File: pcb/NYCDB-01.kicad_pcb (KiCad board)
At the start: 2 copper layers, 266 parts, among them J1 AUDIO_JACK, P1 CONN_BATT, P2 USB_OTG, Q1 Q_PMOS_GSD, SW1 SW_POWER, SW2 SW_RESET, U1 CS5361, U10 OPA4134, U11 TPA6120A2, U12 24C16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

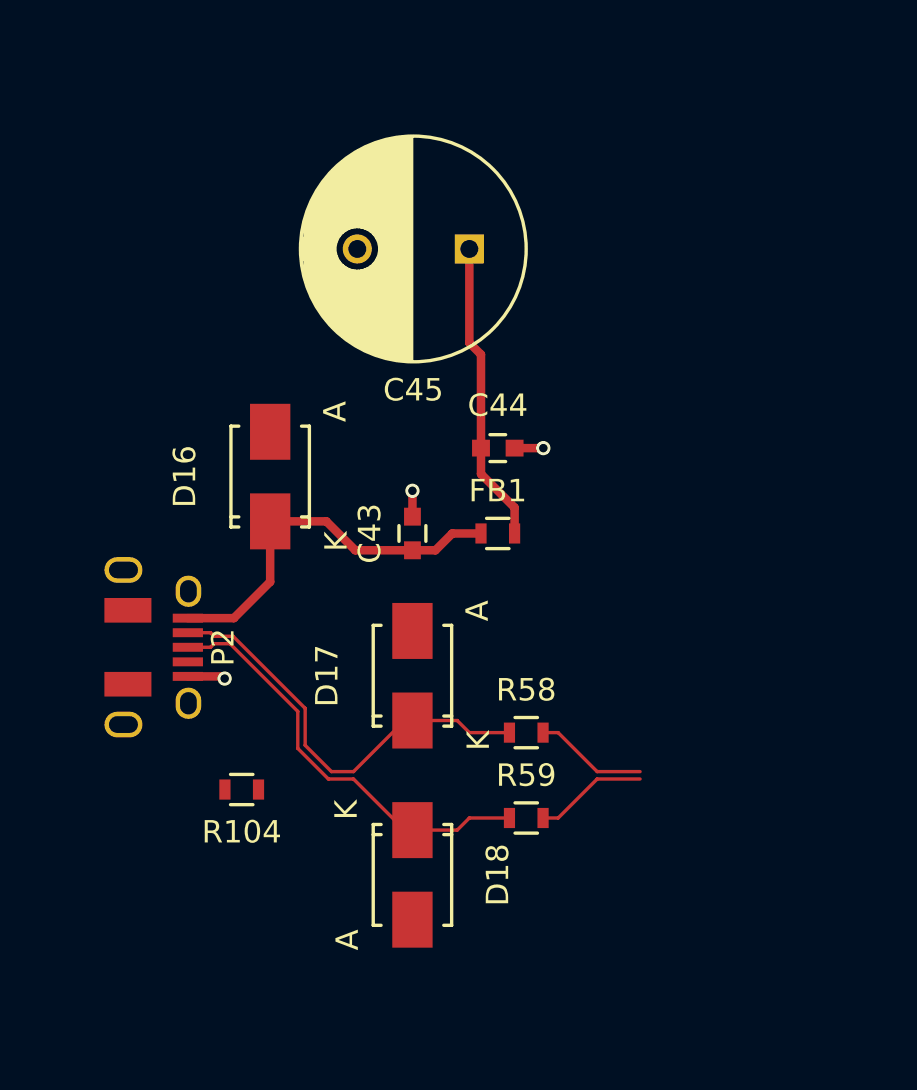
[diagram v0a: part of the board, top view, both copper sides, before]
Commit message: Worked on the USB connection
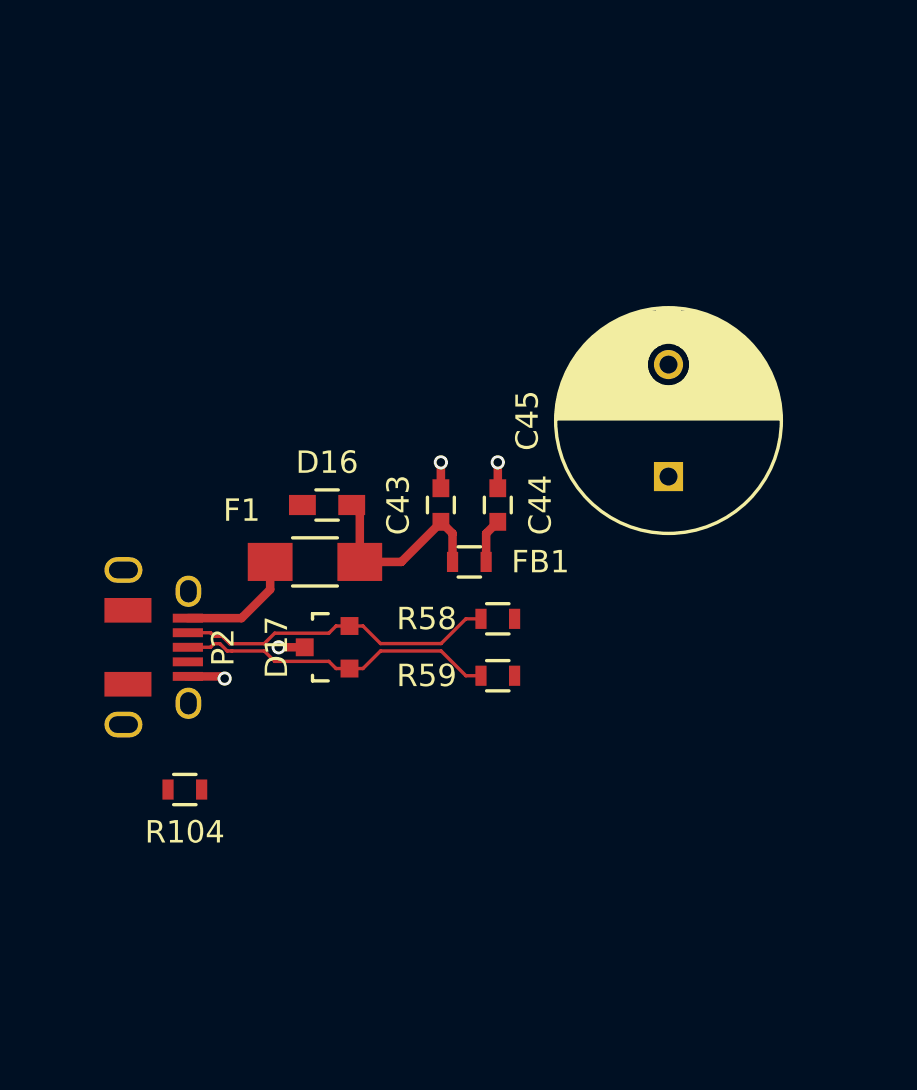
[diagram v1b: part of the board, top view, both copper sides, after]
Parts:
- removed D18: SMAJ5.0CA, Diodes_SMD:SMA_Standard
- added F1: 1206L150, Resistors_SMD:R_1206_HandSoldering, F.Cu at (172.2, 191.8)
- D16: value SMAJ5.0CA -> V5.5MLA0603H; footprint Diodes_SMD:SMA_Standard -> Resistors_SMD:R_0603_HandSoldering
- D17: value SMAJ5.0CA -> TVS_SOT23; footprint Diodes_SMD:SMA_Standard -> TO_SOT_Packages_SMD:SOT-23
- moved C45 13.5 mm to (188.0, 188.0), turned to 90 degrees
- moved R59 6.48 mm to (180.3, 196.8)
- moved R58 5.24 mm to (180.3, 194.3)
- moved D17 4.02 mm to (172.7, 195.6)
- moved D16 2.84 mm to (172.7, 189.2), turned to 0 degrees
- moved C44 2.54 mm to (180.3, 189.2), turned to 270 degrees
- moved R104 2.54 mm to (166.4, 201.9)
- moved C43 1.80 mm to (177.8, 189.2)
- moved FB1 1.80 mm to (179.1, 191.8), turned to 180 degrees
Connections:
- C44 pad 1: /FT2232D/USB5V -> GND
- C44 pad 2: GND -> /FT2232D/USB5V
- D16 pad 1: Net-(C43-Pad1) -> GNDPWR
- D16 pad 2: GNDPWR -> Net-(C43-Pad1)
- D17 pad 1: /USB Connector/CON_D- -> /USB Connector/CON_D+
- D17 pad 2: GNDPWR -> /USB Connector/CON_D-
- FB1 pad 1: Net-(C43-Pad1) -> /FT2232D/USB5V
- FB1 pad 2: /FT2232D/USB5V -> Net-(C43-Pad1)
- P2 pad 1: Net-(C43-Pad1) -> Net-(F1-Pad1)
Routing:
- net /FT2232D/USB5V: track 19.9 -> 8.37 mm
- net Net-(C43-Pad1): track 17.3 -> 9.07 mm
- net Net-(F1-Pad1): track 0.00 -> 5.44 mm
- net /FT2232D/D-: track 5.05 -> 0.00 mm
- net /FT2232D/D+: track 5.05 -> 0.00 mm
- net /USB Connector/CON_D+: track 19.1 -> 14.4 mm
- net /USB Connector/CON_D-: track 19.1 -> 14.4 mm
- net GNDPWR: track 0.00 -> 1.16 mm, vias 0 -> 1

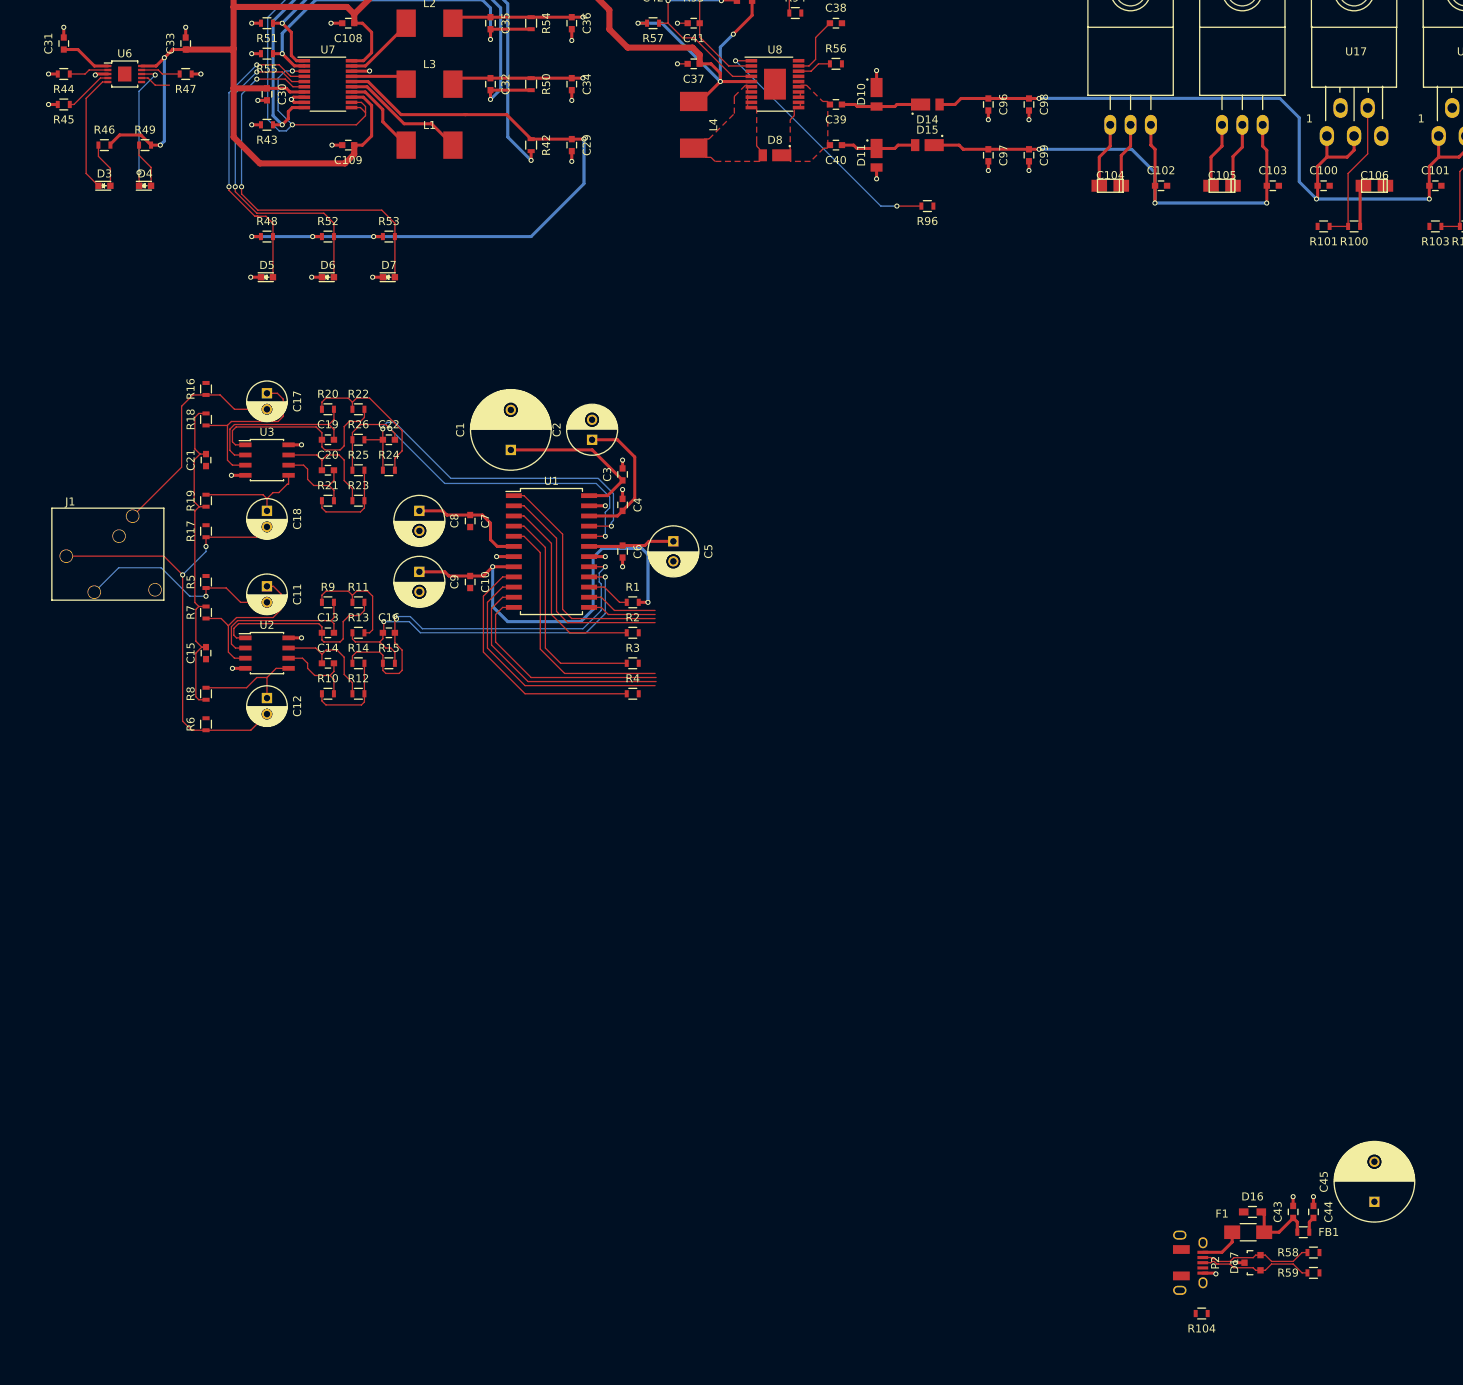
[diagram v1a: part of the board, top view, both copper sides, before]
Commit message: Moved the USB connector to a better spot
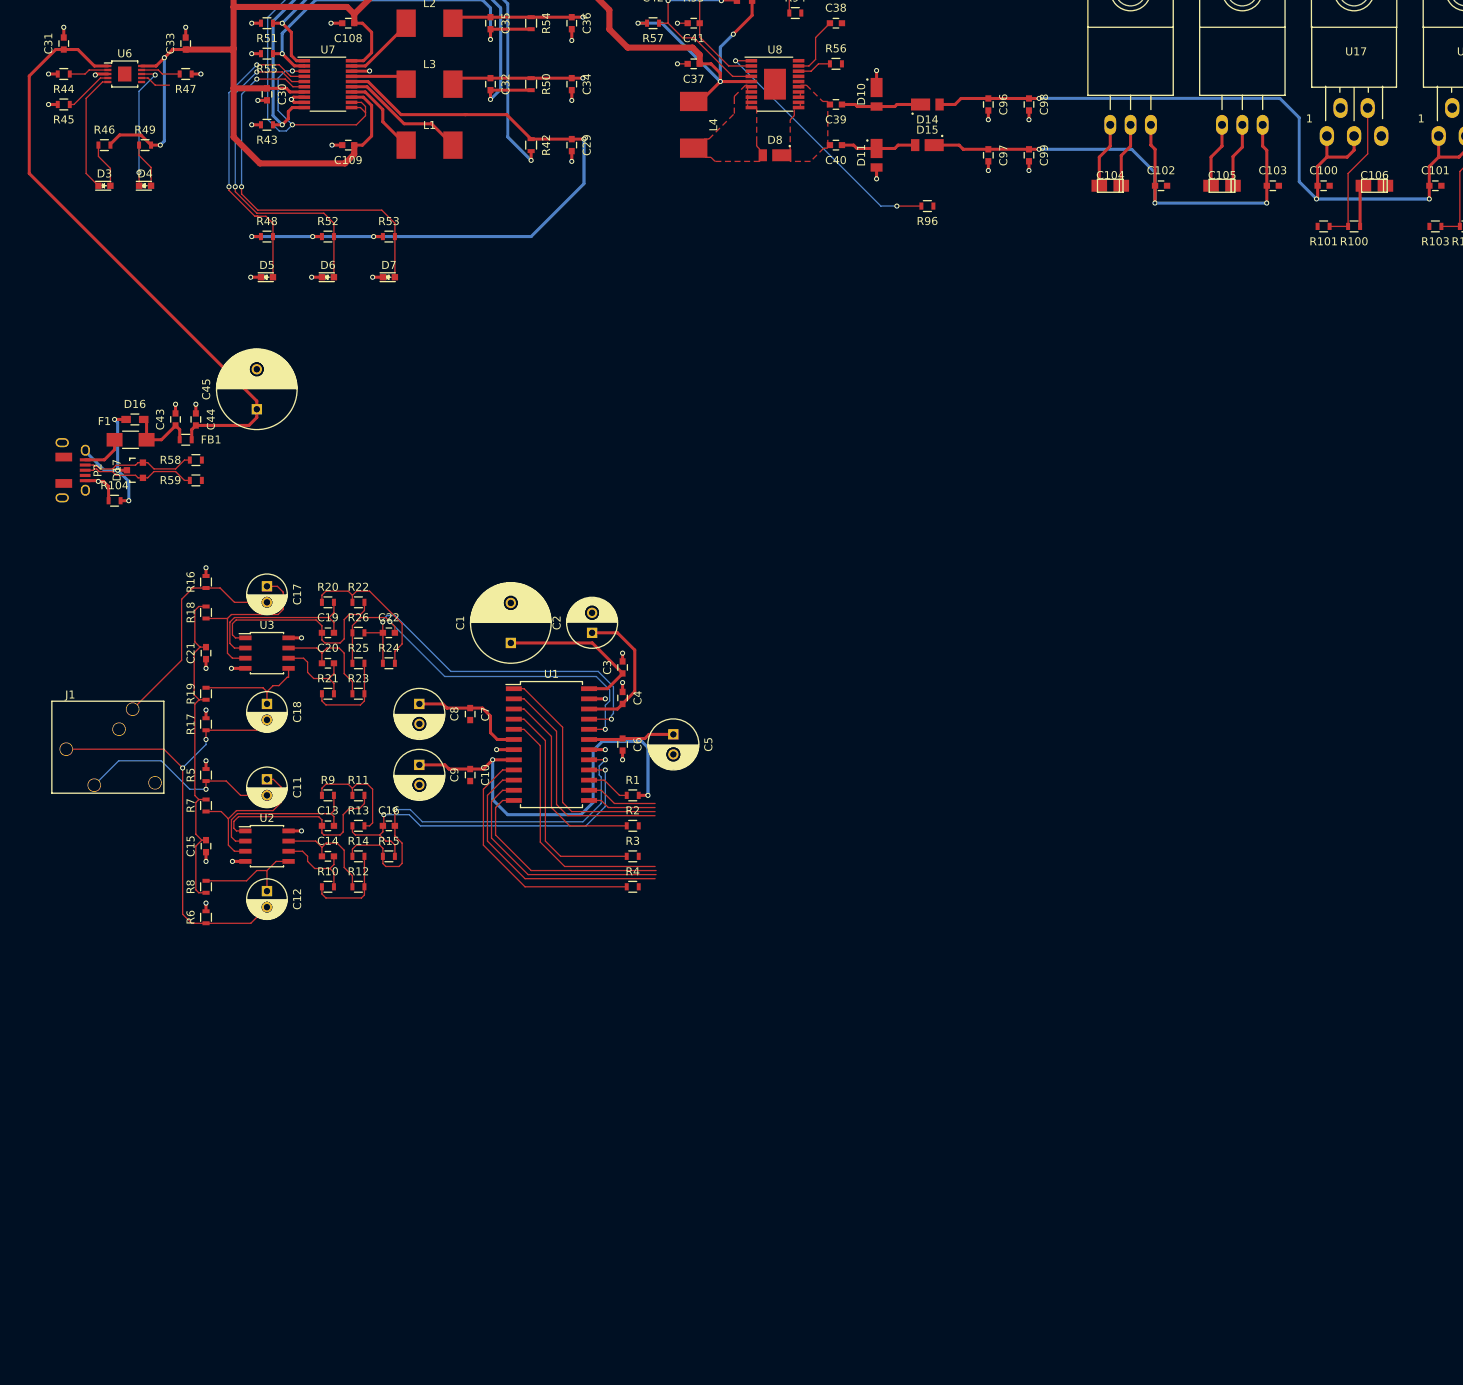
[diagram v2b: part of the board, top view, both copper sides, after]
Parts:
- moved F1 171.3 mm to (32.5, 92.7)
- moved C43 171.3 mm to (38.1, 90.2)
- moved C44 171.3 mm to (40.6, 90.2)
- moved C45 171.3 mm to (48.3, 88.9)
- moved D16 171.3 mm to (33.0, 90.2)
- moved D17 171.3 mm to (33.0, 96.5)
- moved FB1 171.3 mm to (39.4, 92.7)
- moved P2 171.3 mm to (22.7, 96.5)
- moved R58 171.3 mm to (40.6, 95.2)
- moved R59 171.3 mm to (40.6, 97.8)
- moved R104 169.7 mm to (30.5, 100.3), turned to 0 degrees
- moved C10 24.1 mm to (74.9, 134.6)
- moved C18 24.1 mm to (49.5, 125.7)
- moved C19 24.1 mm to (57.1, 116.8)
- moved C2 24.1 mm to (90.2, 116.8)
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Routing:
- net /FT2232D/USB5V: track 8.37 -> 76.6 mm
- net GNDPWR: track 1.16 -> 19.7 mm, vias 1 -> 3
- net GND: track 70.5 -> 80.3 mm, vias 38 -> 44

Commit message: Started laying out FPGA
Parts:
- removed R58, R59: 27, Resistors_SMD:R_0603
- moved C50 328.5 mm to (392.4, 222.5)
- moved C52 328.5 mm to (386.2, 195.4)
- moved C53 328.5 mm to (358.1, 217.8)
- moved C55 328.5 mm to (372.4, 208.0)
- moved C57 328.5 mm to (399.0, 210.9)
- moved C59 328.5 mm to (399.8, 205.1)
- moved C60 328.5 mm to (389.9, 210.6)
- moved C66 328.5 mm to (398.5, 199.3)
- moved C68 328.5 mm to (386.2, 216.4)
- moved C70 328.5 mm to (352.2, 217.8)
- moved R61 328.5 mm to (372.1, 221.5)
- moved R62 328.5 mm to (394.6, 199.3)
- moved R66 328.5 mm to (401.9, 193.5)
- moved R67 328.5 mm to (385.9, 210.6)
- moved R68 328.5 mm to (378.8, 212.7)
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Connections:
- net Net-(R29-Pad1) renamed /FT2232D/USBD-
- net Net-(R30-Pad1) renamed /FT2232D/USBD+
- D17 pad 1: /USB Connector/CON_D+ -> /FT2232D/D+
- D17 pad 2: /USB Connector/CON_D- -> /FT2232D/D-
- P2 pad 2: /USB Connector/CON_D- -> /FT2232D/D-
- P2 pad 3: /USB Connector/CON_D+ -> /FT2232D/D+
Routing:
- net +3V3: track 84.1 -> 372.9 mm, vias 3 -> 23
- net +1V2: track 16.6 -> 105.8 mm, vias 1 -> 6
- net +5V: track 96.4 -> 162.6 mm, vias 4 -> 9
- net GND: track 80.3 -> 129.5 mm, vias 44 -> 78
- net /FT2232D/D-: track 0.00 -> 44.8 mm, vias 0 -> 2
- net /FT2232D/D+: track 0.00 -> 44.7 mm, vias 0 -> 2
- net /FT2232D/USB5V: track 76.6 -> 119.3 mm, vias 0 -> 1
- net Net-(R83-Pad2): track 0.00 -> 37.3 mm
- net Net-(R79-Pad2): track 0.00 -> 35.0 mm
- net Net-(R81-Pad2): track 0.00 -> 25.3 mm
- net Net-(U13-Pad5): track 0.00 -> 24.8 mm
- net Net-(R33-Pad1): track 0.00 -> 23.9 mm, vias 0 -> 2
- net Net-(U4-Pad1): track 0.00 -> 22.3 mm, vias 0 -> 2
- net Net-(R31-Pad1): track 0.00 -> 21.3 mm, vias 0 -> 2
- net /FT2232D/TDO: track 0.00 -> 20.9 mm, vias 0 -> 2
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
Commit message: More work on the FPGA
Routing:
- net Net-(R78-Pad2): track 0.00 -> 37.6 mm, vias 0 -> 2
- net Net-(R77-Pad2): track 0.00 -> 34.7 mm, vias 0 -> 2
- net Net-(D13-Pad2): track 2.31 -> 25.5 mm, vias 0 -> 2
- net Net-(D12-Pad1): track 0.00 -> 19.1 mm, vias 0 -> 2
- net +3V3: track 372.9 -> 391.9 mm, vias 23 -> 29
- net Net-(R97-Pad2): track 11.7 -> 28.1 mm
- net Net-(R81-Pad2): track 25.3 -> 35.0 mm, vias 0 -> 2
- net Net-(U13-Pad5): track 24.8 -> 33.5 mm, vias 0 -> 2
- net Net-(R84-Pad1): track 0.00 -> 7.85 mm, vias 0 -> 2
- net GND: track 129.5 -> 136.0 mm, vias 78 -> 82
- net Net-(R75-Pad2): track 0.00 -> 5.72 mm
- net Net-(R79-Pad2): track 35.0 -> 40.6 mm
- net Net-(R86-Pad2): track 0.00 -> 5.26 mm
- net Net-(R99-Pad1): track 0.00 -> 4.64 mm
- net Net-(R83-Pad2): track 37.3 -> 34.7 mm

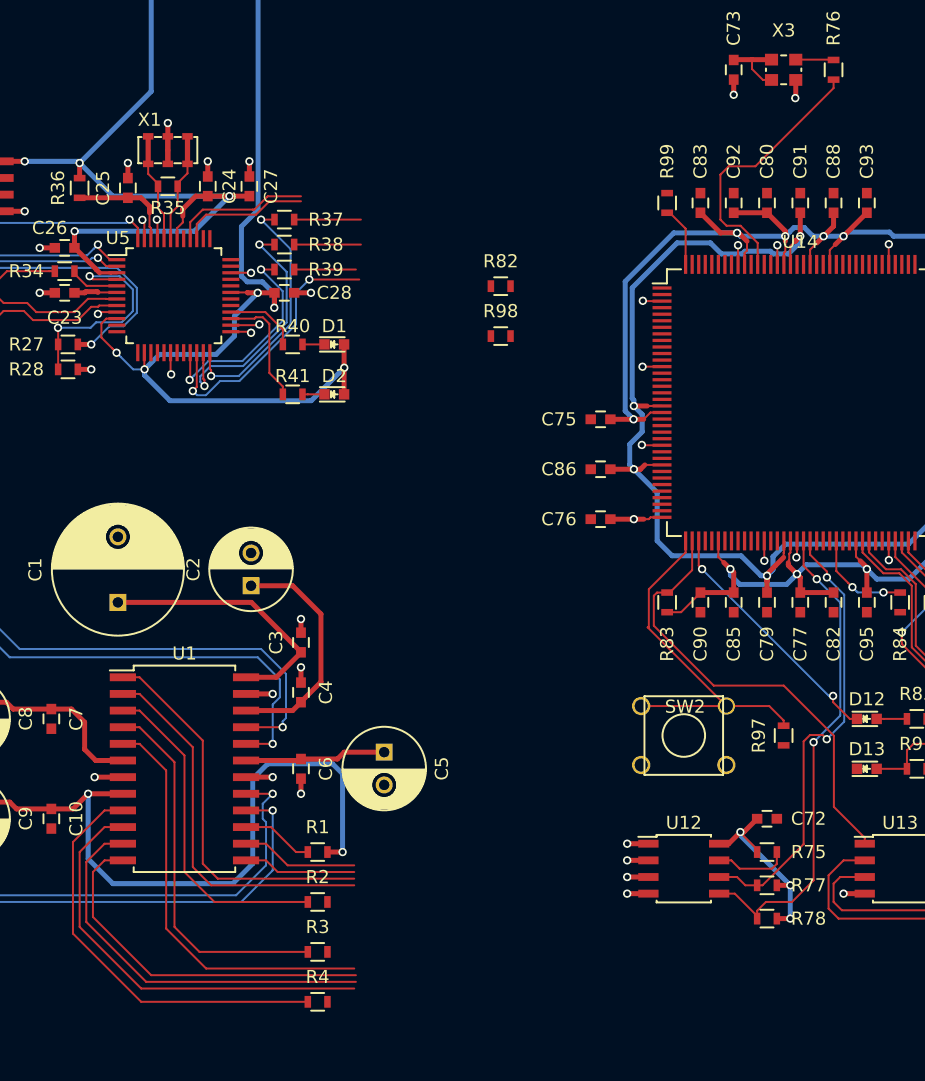
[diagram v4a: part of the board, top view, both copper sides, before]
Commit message: Reworking some of the ADC->FPGA traces
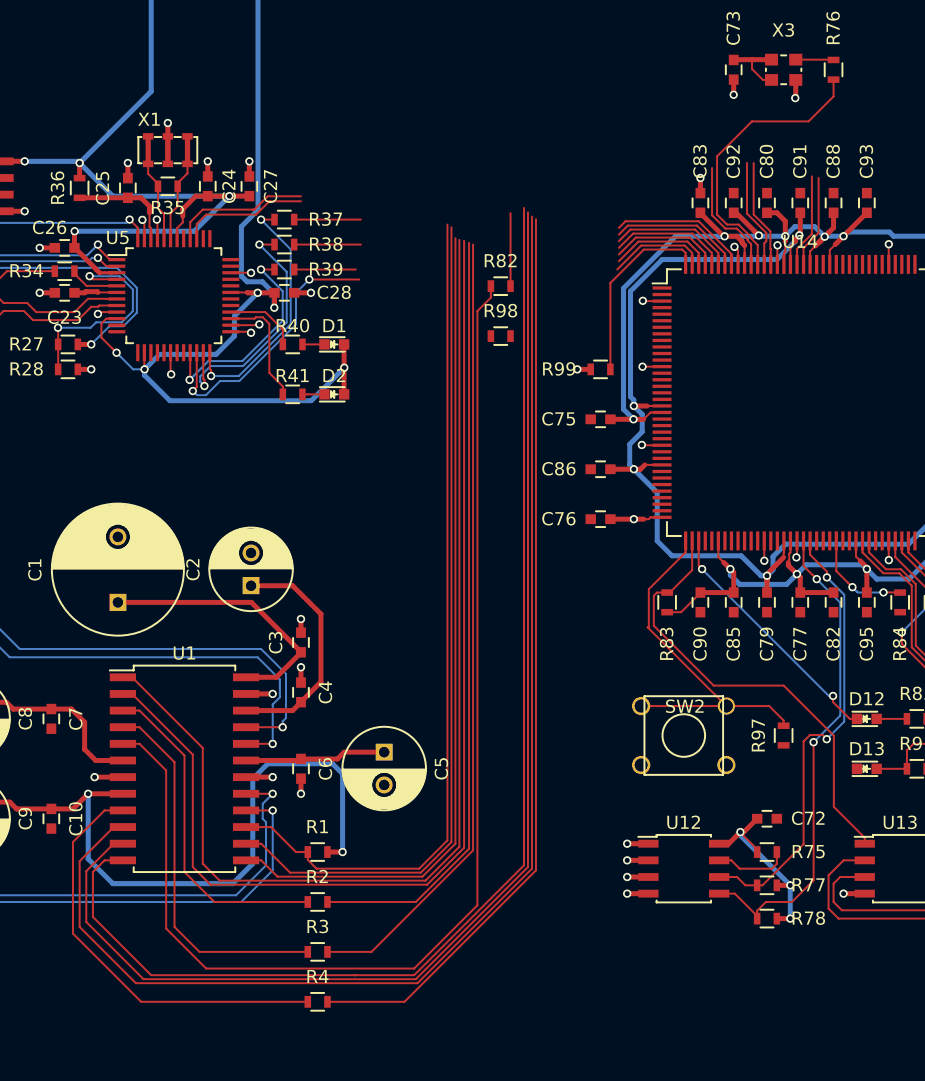
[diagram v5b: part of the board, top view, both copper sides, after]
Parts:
- moved R99 13.7 mm to (116.8, 100.3), turned to 180 degrees
- turned R82 to 180 degrees
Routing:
- net /CS5361 ADC/ADC_SDO: track 0.00 -> 76.8 mm
- net /CS5361 ADC/ADC_HPF: track 30.4 -> 106.1 mm
- net /CS5361 ADC/ADC_MDIV: track 32.7 -> 108.2 mm
- net /CS5361 ADC/ADC_I2S_LJ: track 28.0 -> 103.1 mm
- net /CS5361 ADC/ADC_SCLK: track 0.00 -> 68.8 mm
- net /CS5361 ADC/ADC_OVFL: track 5.50 -> 72.9 mm
- net /CS5361 ADC/ADC_M1: track 8.94 -> 75.1 mm
- net /CS5361 ADC/ADC_LRCLK: track 0.00 -> 65.9 mm
- net /CS5361 ADC/ADC_M0: track 8.62 -> 73.8 mm
- net /CS5361 ADC/ADC_MS: track 29.1 -> 93.6 mm
- net /CS5361 ADC/ADC_RST: track 29.5 -> 92.2 mm
- net /CS5361 ADC/ADC_MCLK: track 31.8 -> 90.9 mm
- net Net-(R82-Pad1): track 0.00 -> 14.0 mm
- net Net-(R99-Pad1): track 4.64 -> 14.4 mm
- net GND: track 136.0 -> 138.1 mm, vias 82 -> 84
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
